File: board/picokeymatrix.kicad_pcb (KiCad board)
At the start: 2 copper layers, 122.5 x 55 mm, 55 parts, among them CN1 PJ-3220-Y, J1 Conn_01x12, J10 Conn_01x18, J11 Conn_01x04, J12 Conn_01x04, J13 Conn_01x04, J14 Conn_01x04, J15 Conn_01x04, J16 Conn_01x04, J17 Conn_01x04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

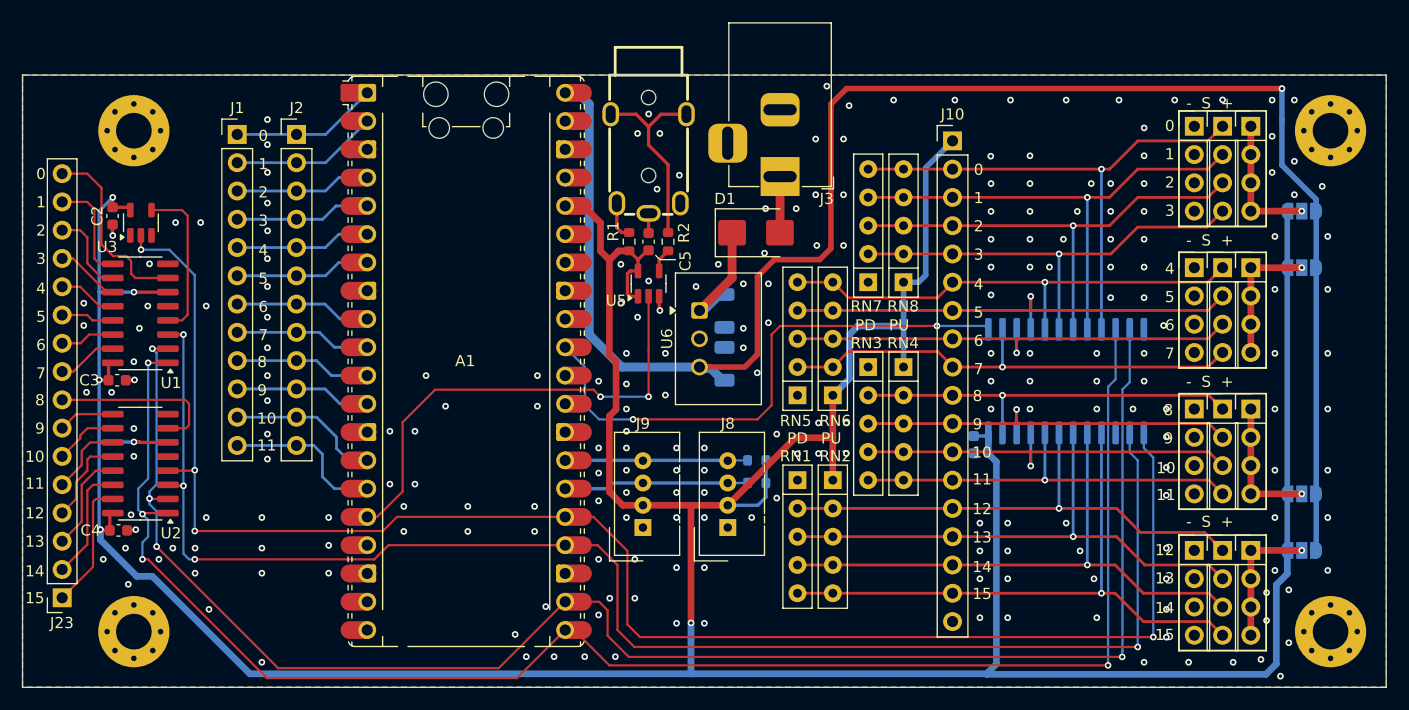
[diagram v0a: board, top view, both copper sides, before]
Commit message: Potmeter pinout, caps on supply
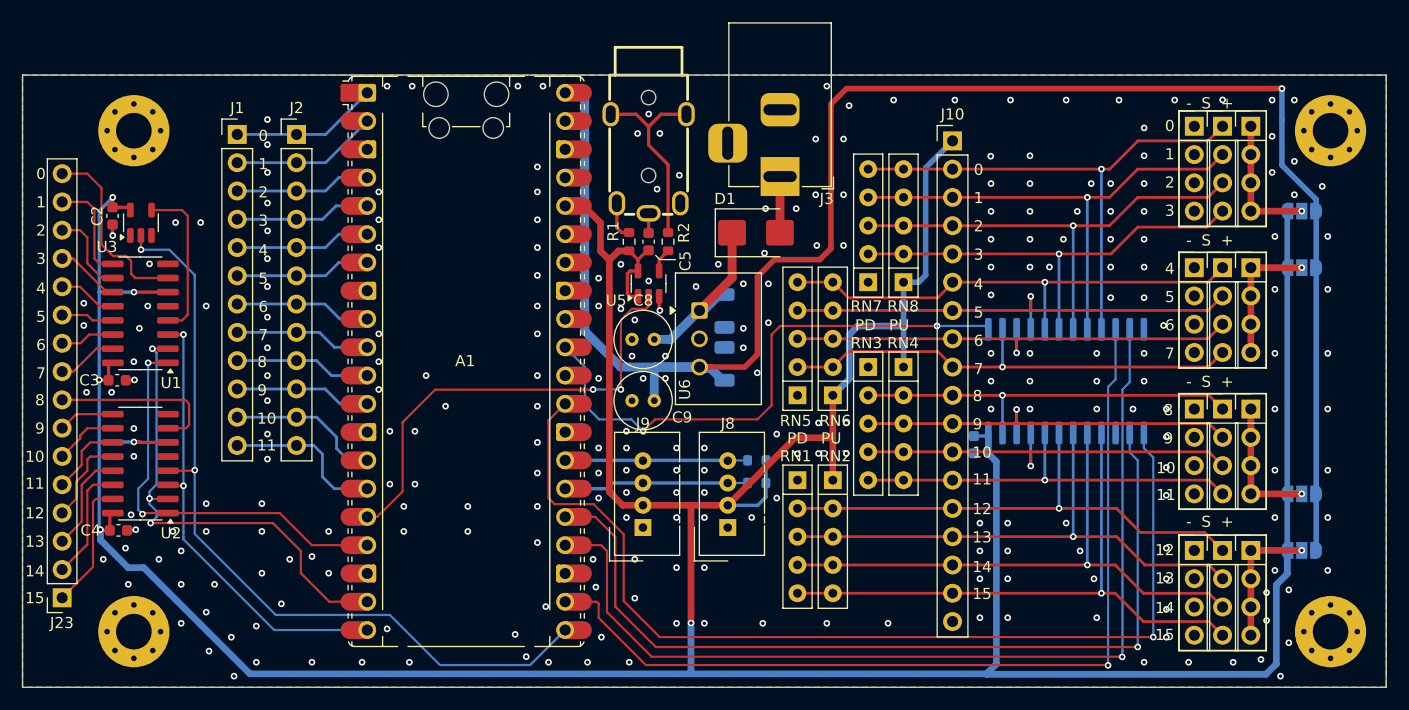
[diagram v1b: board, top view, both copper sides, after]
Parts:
- added C8: TBD, Capacitor_THT:C_Radial_D5.0mm_H7.0mm_P2.00mm, F.Cu at (126.8, 83.8)
- added C9: TBD, Capacitor_THT:C_Radial_D5.0mm_H7.0mm_P2.00mm, F.Cu at (126.8, 89.2)
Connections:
- A1 pad 17: unconnected-(A1-GPIO13-Pad17) -> /KROW_A0
- A1 pad 19: unconnected-(A1-GPIO14-Pad19) -> /KROW_A1
- A1 pad 20: unconnected-(A1-GPIO15-Pad20) -> /KROW_A2
- A1 pad 21: /KROW_A0 -> /KROW_A3
- A1 pad 22: /KROW_A1 -> /PSEL_0
- A1 pad 24: /KROW_A2 -> /PSEL_1
- A1 pad 25: /KROW_A3 -> /PSEL_2
- A1 pad 29: unconnected-(A1-GPIO22-Pad29) -> /PSEL_3
- U7 pad 10: /KROW_A0 -> /PSEL_0
- U7 pad 11: /KROW_A1 -> /PSEL_1
- U7 pad 13: /KROW_A3 -> /PSEL_3
- U7 pad 14: /KROW_A2 -> /PSEL_2
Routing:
- net /KROW_A0: track 146.6 -> 36.5 mm, vias 4 -> 2
- net /KROW_A1: track 147.6 -> 42.4 mm, vias 4 -> 3
- net /KROW_A2: track 135.7 -> 41.1 mm, vias 4 -> 2
- net /PSEL_3: track 0.00 -> 90.8 mm, vias 0 -> 1
- net /PSEL_1: track 0.00 -> 86.3 mm, vias 0 -> 1
- net /PSEL_0: track 0.00 -> 81.5 mm, vias 0 -> 1
- net /PSEL_2: track 0.00 -> 78.7 mm, vias 0 -> 1
- net /KROW_A3: track 146.1 -> 72.2 mm, vias 4 -> 2
- net +5V: track 154.3 -> 161.4 mm
- net Net-(D1-K): track 11.0 -> 16.2 mm
- net /MIDI_OUT: track 42.9 -> 41.4 mm
- net Net-(A1-GPIO26_ADC0): track 50.0 -> 50.9 mm
- net GND: vias 231 -> 267

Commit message: P
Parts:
- C1, U7: moved to F.Cu
- moved C1 15.4 mm to (170.7, 95.1)
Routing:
- net Net-(A1-GPIO26_ADC0): track 50.9 -> 67.1 mm, vias 2 -> 3
- net /PSEL_3: track 90.8 -> 75.1 mm, vias 1 -> 0
- net /PSEL_2: track 78.7 -> 65.0 mm, vias 1 -> 0
- net /PSEL_1: track 86.3 -> 74.8 mm, vias 1 -> 0
- net /PSEL_0: track 81.5 -> 71.9 mm, vias 1 -> 0
- net GND: track 5.69 -> 9.30 mm, vias 267 -> 269
- net +3.3V: track 351.1 -> 348.2 mm, vias 6 -> 7
- net /POT_5: track 43.0 -> 40.7 mm
- net /POT_10: track 36.6 -> 34.3 mm

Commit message: Update
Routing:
- net Net-(A1-GPIO26_ADC0): track 67.1 -> 66.6 mm
- net GND: vias 269 -> 280
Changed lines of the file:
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@@
 		(tags "Grove-1x04")
 		(property "Reference" "J8"
-			(at 0 9.334 0)
+			(at 2.15 -4.153 0)
 			(layer "F.SilkS")
 			(effects
@@
 		(tags "resistor")
 		(property "Reference" "R2"
-			(at -0.8025 -1.425 90)
+			(at -0.1705 -3.112 90)
 			(layer "F.SilkS")
 			(effects
@@
 		(tags "Grove-1x04")
 		(property "Reference" "J9"
-			(at 0 9.334 0)
+			(at 2.33 -4.153 0)
 			(layer "F.SilkS")
 			(effects
@@
 		(tags "resistor")
 		(property "Reference" "R1"
-			(at -0.9295 1.425 90)
+			(at 0.0295 1.588 90)
 			(layer "F.SilkS")
 			(effects
@@
 		(tags "C Radial series Radial pin pitch 2.00mm diameter 5mm height 7mm Non-Polar Electrolytic Capacitor")
 		(property "Reference" "C9"
-			(at -2.5 -1.5 0)
+			(at 4.45 -0.05 90)
 			(layer "F.SilkS")
 			(effects
@@
 		(tags "C Radial series Radial pin pitch 2.00mm diameter 5mm height 7mm Non-Polar Electrolytic Capacitor")
 		(property "Reference" "C8"
-			(at 1 3.5 0)
+			(at 4.55 -0.05 90)
 			(layer "F.SilkS")
 			(effects
@@
 		(tags "SOT TO_SOT_SMD")
 		(property "Reference" "U5"
-			(at -1.524 -2.921 180)
+			(at -1.36 -3.038 180)
 			(layer "F.SilkS")
 			(effects
@@
 		(tags "capacitor")
 		(property "Reference" "C5"
-			(at -1.7375 3.302 270)
+			(at 0.1705 3.302 270)
 			(layer "F.SilkS")
 			(effects
@@
 	)
 	(gr_text "2"
-		(at 71.219762 74.549 -0)
+		(at 71.188762 102.433 -0)
 		(layer "F.SilkS")
 		(effects
@@
 	)
 	(gr_text "10"
-		(at 70.231 94.869 -0)
+		(at 70.2 82.113 -0)
 		(layer "F.SilkS")
 		(effects
@@
 	)
 	(gr_text "13"
-		(at 70.231 102.489 -0)
+		(at 70.2 74.493 -0)
 		(layer "F.SilkS")
 		(effects
@@
 	)
 	(gr_text "14"
-		(at 70.231 105.156 -0)
+		(at 70.2 71.826 -0)
 		(layer "F.SilkS")
 		(effects
@@
 	)
 	(gr_text "9"
-		(at 71.12 92.329 -0)
+		(at 71.089 84.653 -0)
 		(layer "F.SilkS")
 		(effects
@@
 	)
 	(gr_text "7"
-		(at 71.219762 87.376 -0)
+		(at 71.188762 89.606 -0)
 		(layer "F.SilkS")
 		(effects
@@
 	)
 	(gr_text "7"
-		(at 155.448 86.995 -0)
+		(at 150.799762 86.787 -0)
 		(layer "F.SilkS")
 		(effects
@@
 	)
 	(gr_text "1"
-		(at 71.219762 72.009 -0)
+		(at 71.188762 104.973 -0)
 		(layer "F.SilkS")
 		(effects
@@
 	)
 	(gr_text "0"
-		(at 71.219762 69.469 -0)
+		(at 71.188762 107.513 -0)
 		(layer "F.SilkS")
 		(effects
@@
 	)
 	(gr_text "12"
-		(at 70.231 99.949 -0)
+		(at 70.2 77.033 -0)
 		(layer "F.SilkS")
 		(effects
@@
 	)
 	(gr_text "9"
-		(at 155.348238 91.948 -0)
+		(at 150.7 91.74 -0)
 		(layer "F.SilkS")
 		(effects
@@
 	)
 	(gr_text "5"
-		(at 155.448 81.915 -0)
+		(at 150.799762 81.707 -0)
 		(layer "F.SilkS")
 		(effects
@@
 	)
 	(gr_text "11"
-		(at 70.231 97.282 -0)
+		(at 70.2 79.7 -0)
 		(layer "F.SilkS")
 		(effects
@@
 	)
 	(gr_text "15"
-		(at 70.231 107.569 -0)
+		(at 70.2 69.413 -0)
 		(layer "F.SilkS")
 		(effects
@@
 	)
 	(gr_text "3"
-		(at 71.219762 77.089 -0)
+		(at 71.188762 99.893 -0)
 		(layer "F.SilkS")
 		(effects
@@
 	)
 	(gr_text "6"
-		(at 71.219762 84.836 -0)
+		(at 71.188762 92.146 -0)
 		(layer "F.SilkS")
 		(effects
@@
 	)
 	(gr_text "4"
-		(at 71.219762 79.756 -0)
+		(at 71.188762 97.226 -0)
 		(layer "F.SilkS")
 		(effects
@@
 	)
 	(gr_text "8"
-		(at 155.348238 89.408 -0)
+		(at 150.7 89.2 -0)
 		(layer "F.SilkS")
 		(effects
@@
 	)
 	(gr_text "8"
-		(at 71.12 89.789 -0)
+		(at 71.089 87.193 -0)
 		(layer "F.SilkS")
 		(effects
@@
 	)
 	(gr_text "6"
-		(at 155.448 84.455 -0)
+		(at 150.799762 84.247 -0)
 		(layer "F.SilkS")
 		(effects
@@
 	)
 	(gr_text "5"
-		(at 71.219762 82.296 -0)
+		(at 71.188762 94.686 -0)
 		(layer "F.SilkS")
 		(effects
@@
 	)
 	(via
+		(at 131.25 92)
+		(size 0.6)
+		(drill 0.3)
+		(layers "F.Cu" "B.Cu")
+		(free yes)
+		(net 3)
+	)
+	(via
 		(at 143.75 65.75)
 		(size 0.6)
@@
 	)
 	(via
+		(at 137.3 90.9)
+		(size 0.6)
+		(drill 0.3)
+		(layers "F.Cu" "B.Cu")
+		(free yes)
+		(net 3)
+	)
+	(via
 		(at 75.75 88.5)
 		(size 0.6)
@@
 	)
 	(via
+		(at 128.75 90.1)
+		(size 0.6)
+		(drill 0.3)
+		(layers "F.Cu" "B.Cu")
+		(free yes)
+		(net 3)
+	)
+	(via
 		(at 97.5 104.75)
 		(size 0.6)
@@
 	)
 	(via
+		(at 134.4 92.05)
+		(size 0.6)
+		(drill 0.3)
+		(layers "F.Cu" "B.Cu")
+		(free yes)
+		(net 3)
+	)
+	(via
 		(at 170.75 64.75)
 		(size 0.6)
@@
 	)
 	(via
+		(at 134.4 90.1)
+		(size 0.6)
+		(drill 0.3)
+		(layers "F.Cu" "B.Cu")
+		(free yes)
+		(net 3)
+	)
+	(via
 		(at 87.25 105.75)
 		(size 0.6)
@@
 	)
 	(via
+		(at 128.75 92)
+		(size 0.6)
+		(drill 0.3)
+		(layers "F.Cu" "B.Cu")
+		(free yes)
+		(net 3)
+	)
+	(via
 		(at 103 92)
 		(size 0.6)
@@
 	)
 	(via
+		(at 138.1 87.5)
+		(size 0.6)
+		(drill 0.3)
+		(layers "F.Cu" "B.Cu")
+		(free yes)
+		(net 3)
+	)
+	(via
 		(at 92 64)
 		(size 0.6)
@@
 	)
 	(via
+		(at 131.3 90.1)
+		(size 0.6)
+		(drill 0.3)
+		(layers "F.Cu" "B.Cu")
+		(free yes)
+		(net 3)
+	)
+	(via
 		(at 131.25 97.5)
 		(size 0.6)
@@
 	)
 	(via
+		(at 138.05 85)
+		(size 0.6)
+		(drill 0.3)
+		(layers "F.Cu" "B.Cu")
+		(free yes)
+		(net 3)
+	)
+	(via
 		(at 92 89.25)
 		(size 0.6)
@@
 	)
 	(via
+		(at 136 89.7)
+		(size 0.6)
+		(drill 0.3)
+		(layers "F.Cu" "B.Cu")
+		(free yes)
+		(net 3)
+	)
+	(via
 		(at 174.75 112.75)
 		(size 0.6)
@@
 	)
 	(via
+		(at 121.7 90.2)
+		(size 0.6)
+		(drill 0.3)
+		(layers "F.Cu" "B.Cu")
+		(free yes)
+		(net 3)
+	)
+	(via
 		(at 143.75 70.75)
 		(size 0.6)
@@
 	)
 	(segment
-		(start 171.7 82.4)
-		(end 171.8 82.5)
+		(start 120.9 89.1)
+		(end 120.4 88.6)
 		(width 0.2)
 		(layer "B.Cu")
@@
 	)
 	(segment
-		(start 124.682 90.932)
-		(end 121.793 90.932)
+		(start 171.7 82.4)
+		(end 171.8 82.5)
 		(width 0.2)
 		(layer "B.Cu")
@@
 	(segment
 		(start 125.75 92)
-		(end 124.682 90.932)
+		(end 122.85 89.1)
 		(width 0.2)
 		(layer "B.Cu")
@@
 	)
 	(segment
-		(start 121.793 90.932)
-		(end 120.523 89.662)
+		(start 120.4 86.11)
+		(end 118.745 84.455)
 		(width 0.2)
 		(layer "B.Cu")
@@
 	)
 	(segment
-		(start 120.523 86.233)
-		(end 118.745 84.455)
+		(start 122.85 89.1)
+		(end 120.9 89.1)
 		(width 0.2)
 		(layer "B.Cu")
@@
 	)
 	(segment
-		(start 120.523 89.662)
-		(end 120.523 86.233)
+		(start 120.4 88.6)
+		(end 120.4 86.11)
 		(width 0.2)
 		(layer "B.Cu")

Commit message: Fix RPi pico footprint for TH mounting
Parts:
- A1: footprint Module:RaspberryPi_Pico_Common_Unspecified -> Module:RaspberryPi_Pico_Common_THT
- moved A1 25.7 mm to (100.9, 61.6)
